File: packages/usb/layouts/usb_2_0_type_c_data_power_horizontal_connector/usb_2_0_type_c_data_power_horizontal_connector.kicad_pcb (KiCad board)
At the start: 2 copper layers, 6 parts

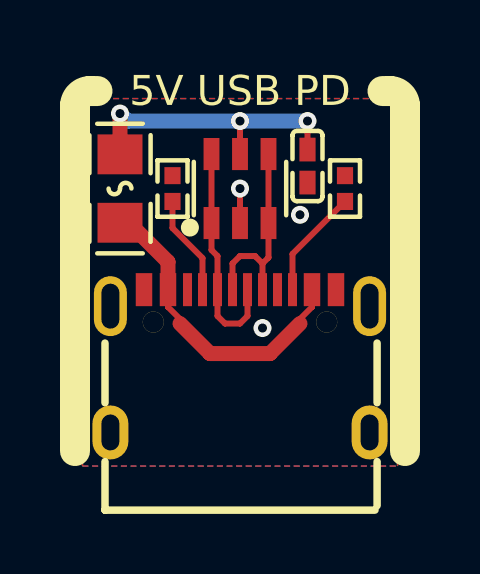
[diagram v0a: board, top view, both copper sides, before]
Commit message: Add vertical usb connector option (#33)
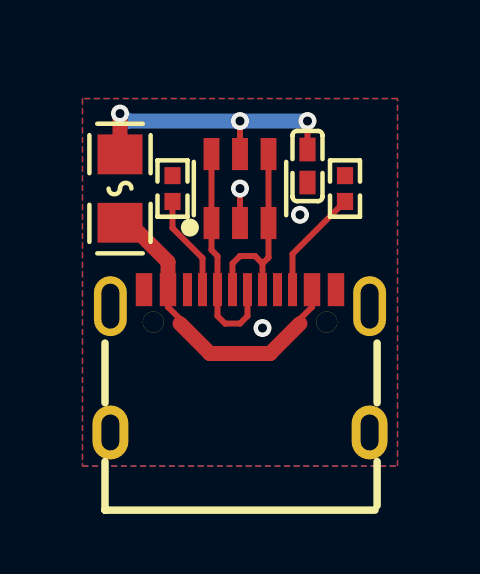
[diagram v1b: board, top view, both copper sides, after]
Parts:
- removed USB1: , atopile:USB-C-SMD_TYPE-C-6PIN-2MD-073-1d78f0
- added X1: , atopile:USB-C-SMD_TYPE-C-6PIN-2MD-073-1d78f0, F.Cu at (0.00, 0.00)
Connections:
- R1 pad 1: CC1 -> line-2
- R2 pad 1: CC2 -> line-1
- U1 pad 3: line-1 -> line-5
- U1 pad 4: line-1 -> line-5
- U2 pad 1: VBUS -> hv-1
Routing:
- net hv-1: track 0.00 -> 10.5 mm
- net VBUS: track 10.5 -> 0.00 mm
- net line-5: track 0.00 -> 6.68 mm
- net CC2: track 3.66 -> 0.00 mm
- net line-2: track 0.00 -> 3.35 mm
- net CC1: track 3.35 -> 0.00 mm
- net line-1: track 6.68 -> 3.66 mm
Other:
- board text removed: "5V USB PD"

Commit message: WIP update usb
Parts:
- C1: footprint atopile:C0402-b3ef17 -> Samsung_Electro_Mechanics_CL05B104KO5NNNC:C0402
- R1, R2: footprint atopile:R0402-56259e -> UNI_ROYAL_0402WGF5101TCE:R0402
- U1: footprint atopile:SOT-23-6_L2.9-W1.6-P0.95-LS2.8-BL-d2c740 -> TECH_PUBLIC_USBLC6_2SC6:SOT-23-6_L2.9-W1.6-P0.95-LS2.8-BL
- U2: footprint atopile:F0805-d5954a -> BHFUSE_BSMD0805_050_15V:F0805
- X1: footprint atopile:USB-C-SMD_TYPE-C-6PIN-2MD-073-1d78f0 -> SHOU_HAN_TYPE_C_16PIN_2MD_073:USB-C-SMD_TYPE-C-6PIN-2MD-073
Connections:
- C1 pad 1: hv -> hv-1
- R1 pad 1: line-2 -> line
- R2 pad 1: line-1 -> line-2
- U1 pad 1: line -> line-5
- U1 pad 3: line-5 -> line-4
- U1 pad 4: line-5 -> line-4
- U1 pad 5: hv -> hv-1
- U1 pad 6: line -> line-5
- U2 pad 1: hv-1 -> hv
- U2 pad 2: hv -> hv-1
- X1 pad : (no net) -> net
- X1 pad 10: line-1 -> line-2
- X1 pad 11: hv-1 -> hv
- X1 pad 2: hv-1 -> hv
- X1 pad 3: line-3 -> line-1
- X1 pad 4: line-2 -> line
- X1 pad 5: line -> line-5
- X1 pad 6: line-5 -> line-4
- X1 pad 7: line -> line-5
- X1 pad 8: line-5 -> line-4
- X1 pad 9: line-4 -> line-3
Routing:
- net line-4: track 0.00 -> 6.68 mm
- net line: track 7.57 -> 3.35 mm
- net line-1: track 3.66 -> 0.00 mm
- net line-5: track 6.68 -> 7.57 mm
- net hv-1: track 10.5 -> 9.76 mm, vias 0 -> 3
- net hv: track 9.76 -> 10.5 mm, vias 3 -> 0

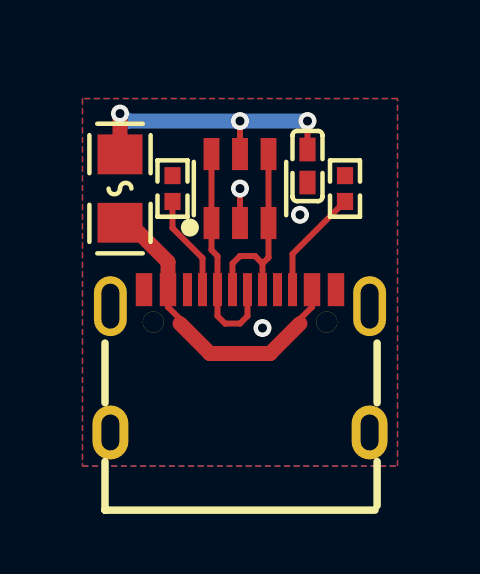
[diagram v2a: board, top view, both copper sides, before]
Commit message: Manually fix fp lib tables
fix some small bugs
fix package only modules (e.g. logos)
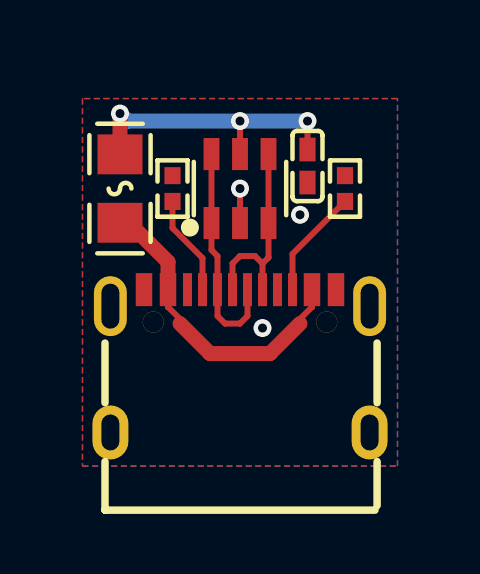
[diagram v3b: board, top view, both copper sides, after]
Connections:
- R1 pad 1: line -> line-3
- R2 pad 1: line-2 -> line
- U1 pad 1: line-5 -> line-4
- U1 pad 3: line-4 -> line-2
- U1 pad 4: line-4 -> line-2
- U1 pad 6: line-5 -> line-4
- X1 pad 10: line-2 -> line
- X1 pad 3: line-1 -> line-5
- X1 pad 4: line -> line-3
- X1 pad 5: line-5 -> line-4
- X1 pad 6: line-4 -> line-2
- X1 pad 7: line-5 -> line-4
- X1 pad 8: line-4 -> line-2
- X1 pad 9: line-3 -> line-1
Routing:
- net line-5: track 7.57 -> 0.00 mm
- net line-3: track 0.00 -> 3.35 mm
- net line-2: track 3.66 -> 6.68 mm
- net line-4: track 6.68 -> 7.57 mm

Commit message: rebuild all packages & regenerate images of changed layouts (silk)
Add new scripts for version bump and build (based on atopile/packages)
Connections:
- R1 pad 1: line-3 -> line
- R2 pad 1: line -> line-1
- U1 pad 3: line-2 -> line-5
- U1 pad 4: line-2 -> line-5
- X1 pad 10: line -> line-1
- X1 pad 3: line-5 -> line-3
- X1 pad 4: line-3 -> line
- X1 pad 6: line-2 -> line-5
- X1 pad 8: line-2 -> line-5
- X1 pad 9: line-1 -> line-2
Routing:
- net line-5: track 0.00 -> 6.68 mm
- net line-2: track 6.68 -> 0.00 mm
- net line-1: track 0.00 -> 3.66 mm
- net line-3: track 3.35 -> 0.00 mm
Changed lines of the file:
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@@
     (net 0 "")
     (net 1 "hv-1")
-    (net 2 "line-2")
+    (net 2 "line-5")
     (net 3 "hv")
-    (net 4 "line-5")
-    (net 5 "line")
-    (net 6 "line-1")
+    (net 4 "line-3")
+    (net 5 "line-1")
+    (net 6 "line-2")
     (net 7 "line-4")
-    (net 8 "line-3")
+    (net 8 "line")
     (net 9 "gnd")
     (net 10 "net")
@@
             (size 0.53 1.07)
             (layers "F.Cu" "F.Paste" "F.Mask")
-            (net 2 "line-2")
+            (net 2 "line-5")
         )
         (pad "4" smd rect
@@
             (size 0.53 1.07)
             (layers "F.Cu" "F.Paste" "F.Mask")
-            (net 2 "line-2")
+            (net 2 "line-5")
         )
         (pad "5" smd rect
@@
             (size 0.3 1.1)
             (layers "F.Cu" "F.Mask" "F.Paste")
-            (net 4 "line-5")
+            (net 4 "line-3")
         )
         (pad "4" smd rect
@@
             (size 0.3 1.1)
             (layers "F.Cu" "F.Mask" "F.Paste")
-            (net 8 "line-3")
+            (net 8 "line")
         )
         (pad "5" smd rect
@@
             (size 0.3 1.1)
             (layers "F.Cu" "F.Mask" "F.Paste")
-            (net 2 "line-2")
+            (net 2 "line-5")
         )
         (pad "7" smd rect
@@
             (size 0.3 1.1)
             (layers "F.Cu" "F.Mask" "F.Paste")
-            (net 2 "line-2")
+            (net 2 "line-5")
         )
         (pad "9" smd rect
@@
             (size 0.3 1.1)
             (layers "F.Cu" "F.Mask" "F.Paste")
-            (net 6 "line-1")
+            (net 6 "line-2")
         )
         (pad "10" smd rect
@@
             (size 0.3 1.1)
             (layers "F.Cu" "F.Mask" "F.Paste")
-            (net 5 "line")
+            (net 5 "line-1")
         )
         (pad "11" smd rect
@@
             (size 0.57 0.54)
             (layers "F.Cu" "F.Paste" "F.Mask")
-            (net 8 "line-3")
+            (net 8 "line")
         )
         (model "${KIPRJMOD}/../../parts/UNI_ROYAL_0402WGF5101TCE/R0402_L1.0-W0.5-H0.4.step"
@@
             (size 0.57 0.54)
             (layers "F.Cu" "F.Paste" "F.Mask")
-            (net 5 "line")
+            (net 5 "line-1")
         )
         (model "${KIPRJMOD}/../../parts/UNI_ROYAL_0402WGF5101TCE/R0402_L1.0-W0.5-H0.4.step"

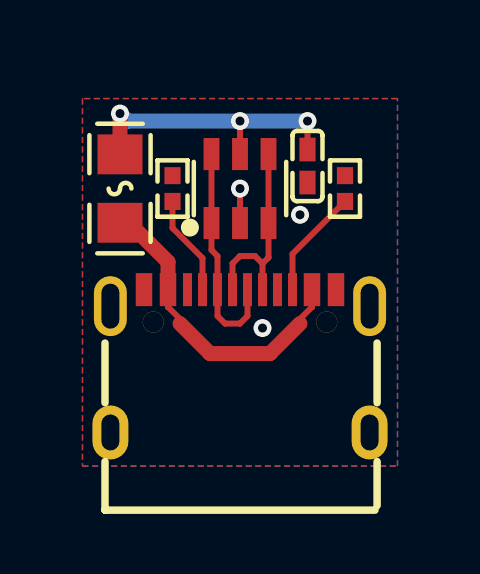
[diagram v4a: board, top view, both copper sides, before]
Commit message: Use packages from packages folder
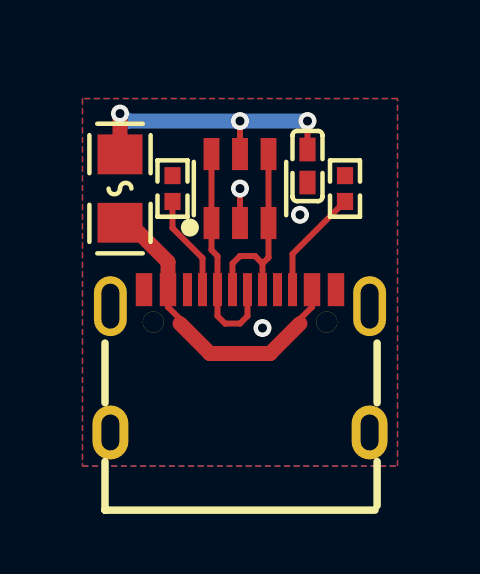
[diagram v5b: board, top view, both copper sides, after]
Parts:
- removed U2: , BHFUSE_BSMD0805_050_15V:F0805
- added F1: , BHFUSE_BSMD0805_050_15V:F0805, F.Cu at (-4.00, -5.75)
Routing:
- net hv-1: vias 3 -> 2
- net (no net): vias 1 -> 2
